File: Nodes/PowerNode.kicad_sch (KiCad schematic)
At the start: 11 parts, among them T1 Conn_01x01, U1 STM32G431KBT6, Y1 ECS-7050MV-080-BN-TR

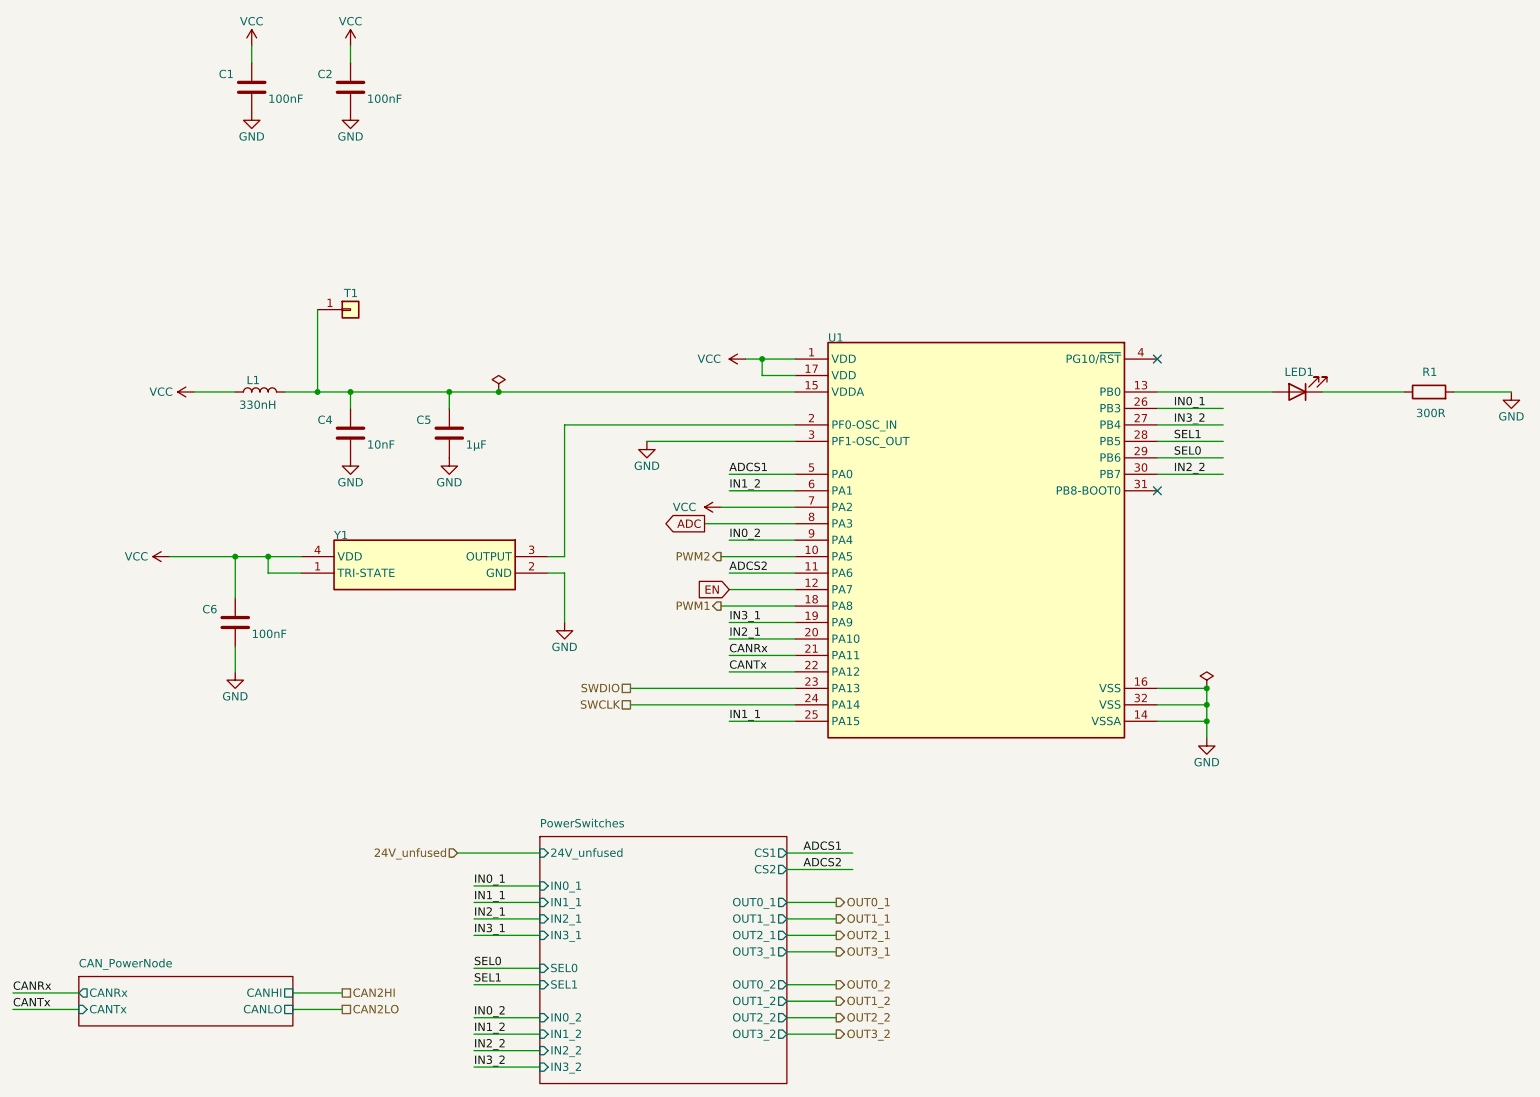
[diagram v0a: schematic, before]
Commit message: Nodes v2.1.2 Improved
- Improved schematic design
- Added two 4.7 uF caps according to the datasheets of the microchips
- Other small changes
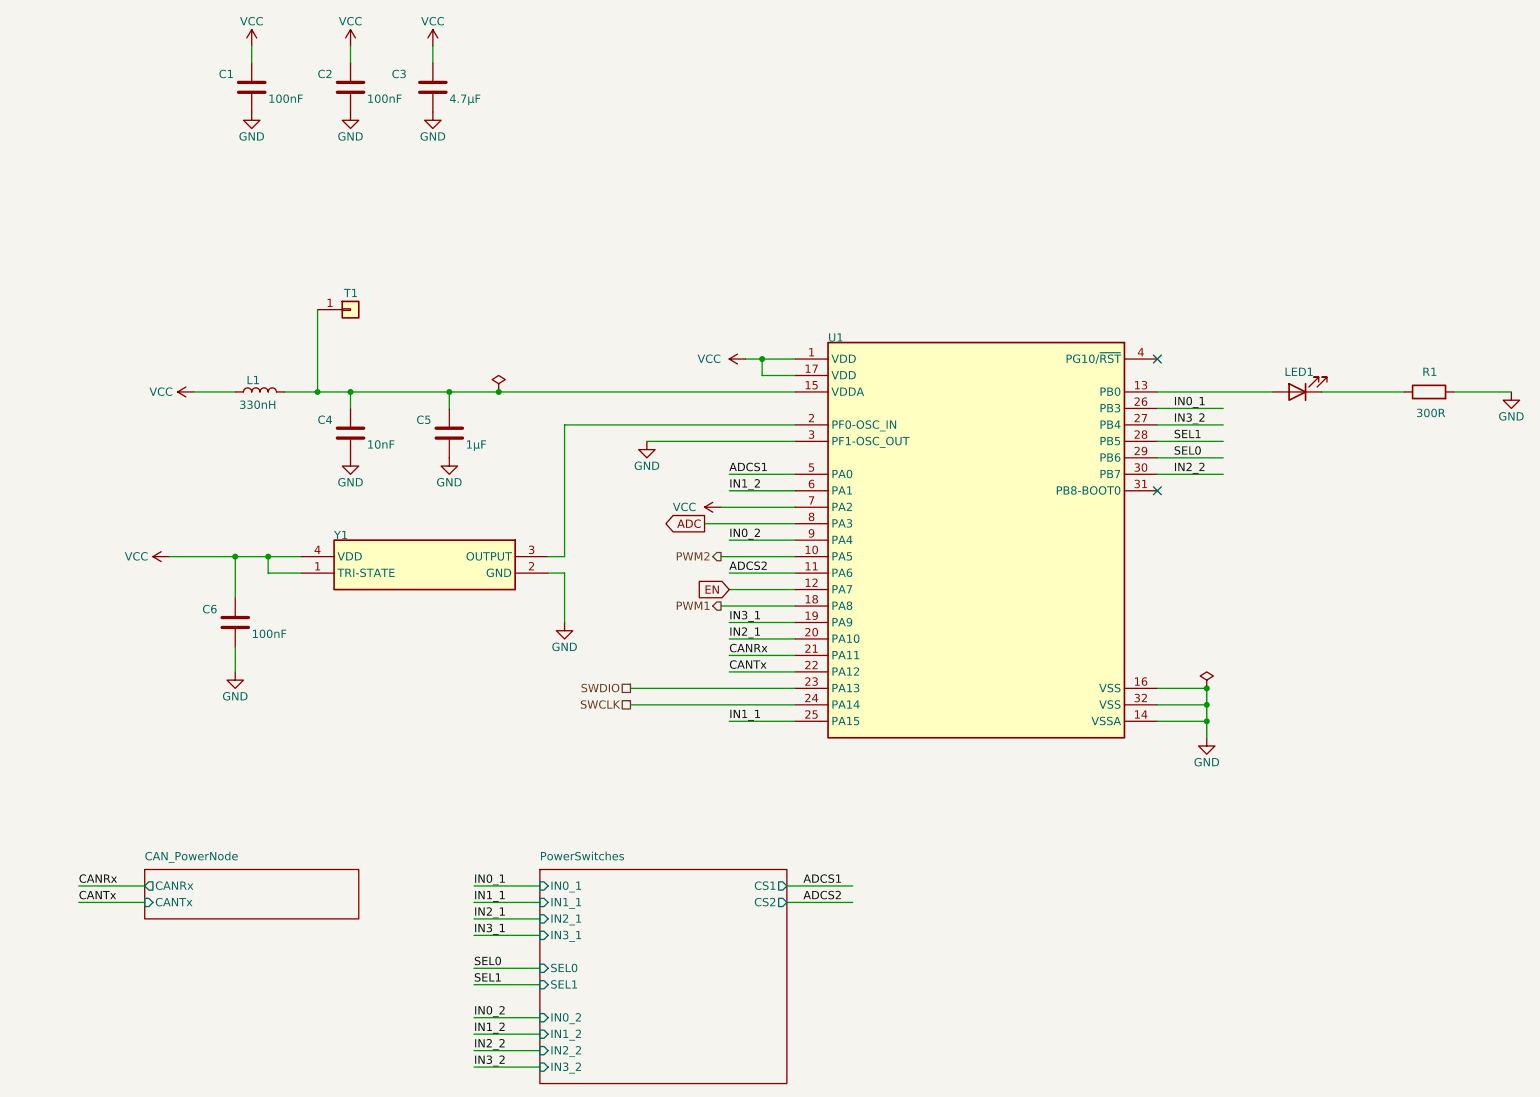
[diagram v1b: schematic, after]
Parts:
- added C3: 4.7µF, Capacitor_SMD:C_0805_2012Metric_Pad1.18x1.45mm_HandSolder, symbol Device:C
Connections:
- net GND: now also C3.2
- net VCC: now also C3.1
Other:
- sheet CAN_PowerNode ports: added none; removed CANHI, CANLO
- sheet PowerSwitches ports: added none; removed 24V_unfused, OUT0_1, OUT0_2, OUT1_1, OUT1_2, OUT2_1, OUT2_2, OUT3_1, OUT3_2

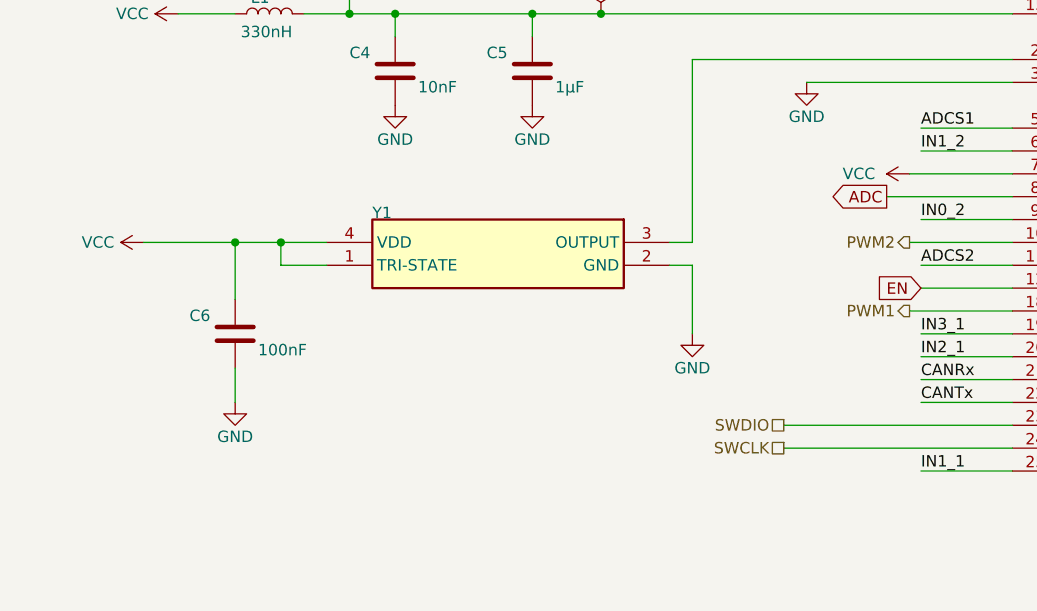
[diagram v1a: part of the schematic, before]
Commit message: Nodes v2.2
- This version not compatible with BOB v.2.1.2 and older!
- Completely new layout design
- New power supply system with new voltage regulators
- New microchip STM32G431RBTx for the Analog Node
- New connection system (instead of 18 pin headers now 8 pin and pins were grouped by functions)
- Reduced size of the board by 5%
- Removed power switch for the Analog Node (because this functionality is now provided by a separate voltage regulator. for a more stable voltage)
- Removable ground from the holes added
- Layer numbers added
- Small improvements of the components information were made
- New oscillator for the Nodes
- Removed CAN1, so now only one CAN connection due to the capabilities of the new microchip
- Other small changes and fixes on the schematic and design
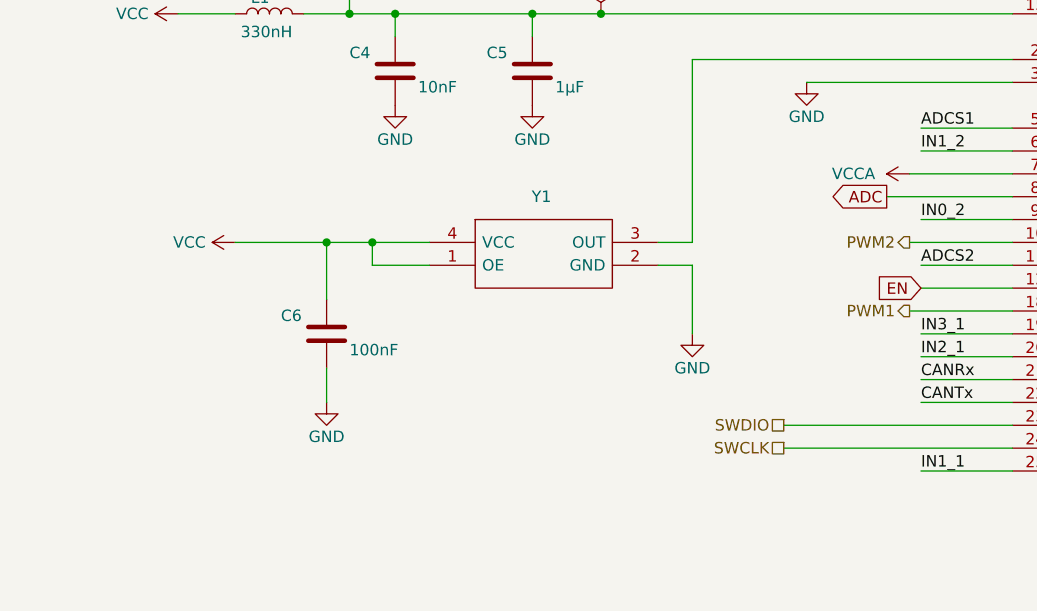
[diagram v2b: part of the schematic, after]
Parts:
- removed Y1: ECS-7050MV-080-BN-TR, SamacSys.PcbLib:ECS7050MV080BNTR, symbol Untitled-altium-import:root_0_ECS-7050MV-080-BN-TR
- added Y1: SG-8018CE_8.0000M-TJHPA3, Oscillator:SG8018CE80000MTJHPA3, symbol Oscillator:SG-8018CE_8.0000M-TJHPA3
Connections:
- net GND: now also Y1.2 (GND)
- net VCC: now also Y1.1 (OE), Y1.4 (VCC); no longer U1.7 (PA2)
- net at U1.2 (PF0-OSC_IN): now also Y1.3 (OUT)
- new net VCCA: U1.7 (PA2)
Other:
- moved on the sheet: C6

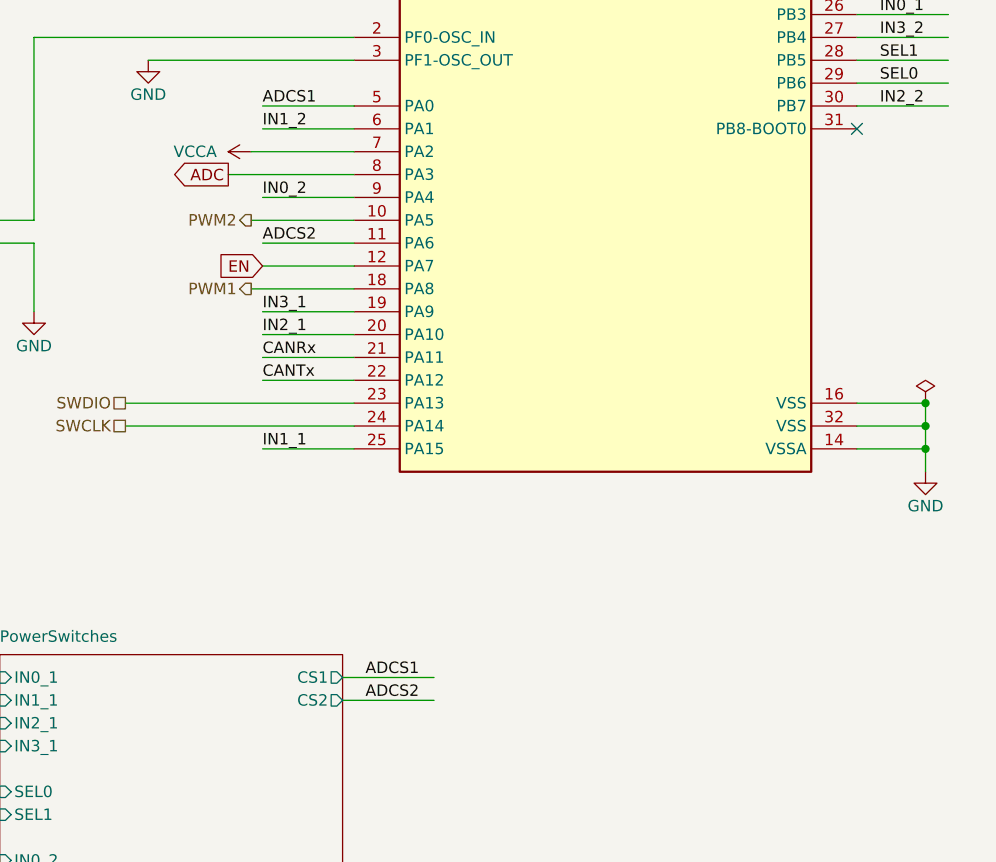
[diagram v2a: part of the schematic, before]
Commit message: Nodes v2.2.2
- Level-Shifter on PWM1 for 24V applications added
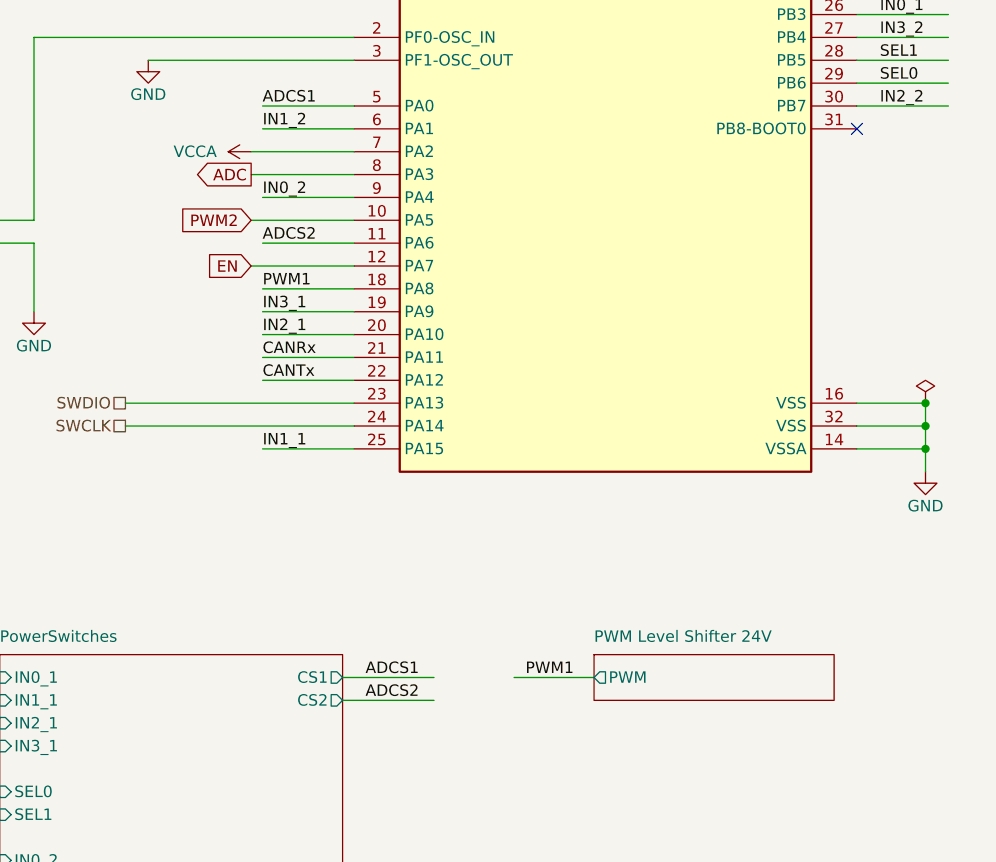
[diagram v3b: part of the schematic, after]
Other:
- added sheet PWM Level Shifter 24V (PWM_24V.kicad_sch)
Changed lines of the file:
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@@
 	(wire
 		(pts
+			(xy 137.16 113.03) (xy 147.32 113.03)
+		)
+		(stroke
+			(width 0)
+			(type default)
+		)
+	)
+	(wire
+		(pts
 			(xy 71.12 119.38) (xy 71.12 123.19)
 		)
@@
 	(wire
 		(pts
+			(xy 165.1 156.21) (xy 173.99 156.21)
+		)
+		(stroke
+			(width 0)
+			(type default)
+		)
+	)
+	(wire
+		(pts
 			(xy 139.7 74.93) (xy 142.24 74.93)
 		)
@@
 	(wire
 		(pts
-			(xy 147.32 113.03) (xy 135.89 113.03)
-		)
-		(stroke
-			(width 0)
-			(type default)
-		)
-	)
-	(wire
-		(pts
 			(xy 73.66 80.01) (xy 68.58 80.01)
 		)
@@
 	(wire
 		(pts
-			(xy 137.16 110.49) (xy 147.32 110.49)
+			(xy 135.89 110.49) (xy 147.32 110.49)
 		)
 		(stroke
@@
 	(wire
 		(pts
-			(xy 147.32 100.33) (xy 133.35 100.33)
+			(xy 147.32 100.33) (xy 135.89 100.33)
 		)
 		(stroke
@@
 		)
 	)
+	(label "PWM1"
+		(at 166.37 156.21 0)
+		(fields_autoplaced yes)
+		(effects
+			(font
+				(size 1.27 1.27)
+			)
+			(justify left bottom)
+		)
+	)
 	(label "CANRx"
 		(at 137.16 120.65 0)
@@
 		)
 	)
+	(label "PWM1"
+		(at 137.16 113.03 0)
+		(fields_autoplaced yes)
+		(effects
+			(font
+				(size 1.27 1.27)
+			)
+			(justify left bottom)
+		)
+	)
 	(label "IN0_2"
 		(at 137.16 102.87 0)
@@
 	(global_label "EN"
 		(shape input)
-		(at 137.16 110.49 180)
+		(at 135.89 110.49 180)
 		(fields_autoplaced yes)
 		(effects
@@
 		)
 		(property "Intersheetrefs" "${INTERSHEET_REFS}"
-			(at 131.6953 110.49 0)
+			(at 130.4253 110.49 0)
 			(effects
 				(font
@@
 	(global_label "ADC"
 		(shape output)
-		(at 133.35 100.33 180)
+		(at 135.89 100.33 180)
 		(fields_autoplaced yes)
 		(effects
@@
 		)
 		(property "Intersheetrefs" "${INTERSHEET_REFS}"
-			(at 126.7362 100.33 0)
+			(at 129.2762 100.33 0)
 			(effects
 				(font
@@
 		)
 	)
-	(hierarchical_label "PWM2"
-		(shape output)
+	(global_label "PWM2"
+		(shape input)
 		(at 135.89 105.41 180)
 		(fields_autoplaced yes)
@@
 			(justify right)
 		)
+		(property "Intersheetrefs" "${INTERSHEET_REFS}"
+			(at 127.5225 105.41 0)
+			(effects
+				(font
+					(size 1.27 1.27)
+				)
+				(justify right)
+				(hide yes)
+			)
+		)
 	)
 	(hierarchical_label "SWDIO"
@@
 		)
 	)
-	(hierarchical_label "PWM1"
-		(shape output)
-		(at 135.89 113.03 180)
-		(fields_autoplaced yes)
-		(effects
-			(font
-				(size 1.27 1.27)
-			)
-			(justify right)
-		)
-	)
 	(hierarchical_label "SWCLK"
 		(shape passive)
@@
 				)
 			)
+		)
+	)
+	(sheet
+		(at 173.99 153.67)
+		(size 26.67 5.08)
+		(stroke
+			(width 0)
+			(type solid)
+			(color 128 0 0 1)
+		)
+		(fill
+			(color 128 255 128 1.0000)
+		)
+		(property "Sheetname" "PWM Level Shifter 24V"
+			(at 173.99 152.4 0)
+			(effects
+				(font
+					(size 1.27 1.27)
+				)
+				(justify left bottom)
+			)
+		)
+		(property "Sheetfile" "PWM_24V.kicad_sch"
+			(at 173.99 153.67 0)
+			(effects
+				(font
+					(size 1.27 1.27)
+				)
+				(justify left bottom)
+				(hide yes)
+			)
+		)
+		(pin "PWM" output
+			(at 173.99 156.21 180)
+			(effects
+				(font
+					(size 1.27 1.27)
+				)
+				(justify left)
+			)
+		)
+		(instances
+			(project "Nodes"
+				(path "/7f1aa41b-970a-42cc-8701-1d90e3bd89a6/0c7bf7f0-7f1e-40ac-a6a8-46292d6f8ac7"
+					(page "15")
+				)
+			)
